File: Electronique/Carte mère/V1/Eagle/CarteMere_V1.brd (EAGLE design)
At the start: 95 x 80.1 mm, 25 parts, among them J100 BP_Rouge, J101 BP Jaune, J102 BP Vert, J600 LED_VERTE, J601 LED_JAUNE, J602 LED_ROUGE, Q500 SI2303DS, Q501 SI2302DS, U200 FIREBEETLE-ESP32-DFR0478, U300 RTC_ADA-3295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

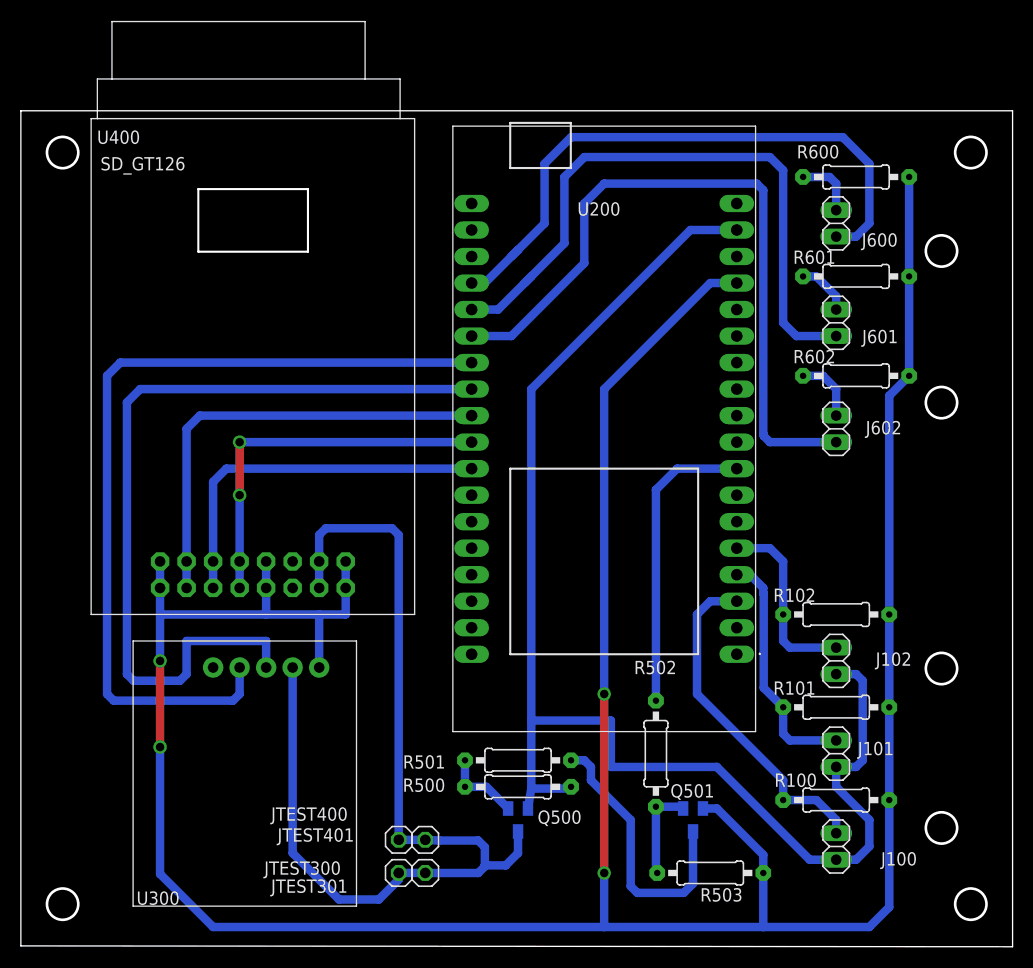
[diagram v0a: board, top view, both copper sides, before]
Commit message: Modificaiton du diamètre perçage vis et recréation des fichiers gerbers
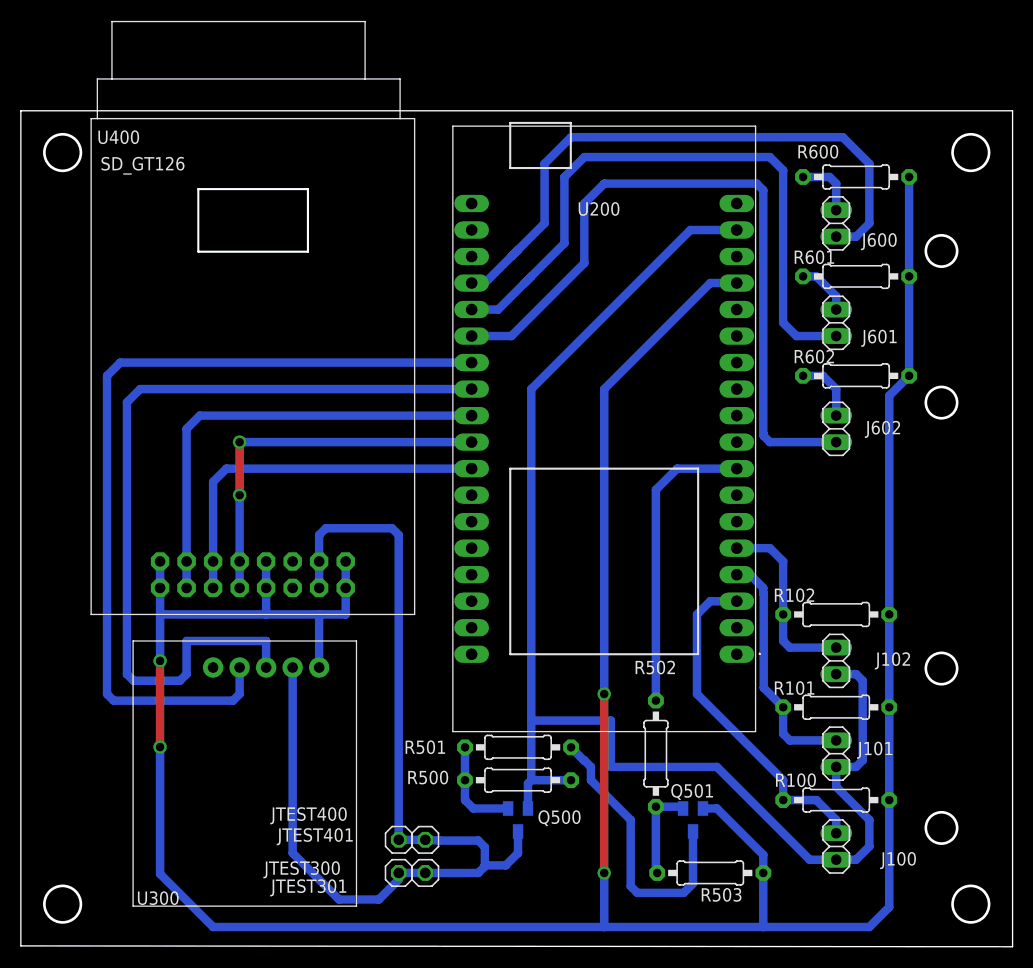
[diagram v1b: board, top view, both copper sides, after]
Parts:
- moved R501 1.24 mm to (47.6, 19.0)
- moved R500 0.63 mm to (47.6, 15.9)
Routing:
- net N$7: track 7.53 -> 9.52 mm
- net DQ501: track 26.8 -> 27.3 mm
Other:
- outline, holes or cut-outs redrawn
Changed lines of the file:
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@@
 <setting verticaltext="up"/>
 </settings>
-<grid distance="50" unitdist="mil" unit="mil" style="lines" multiple="1" display="no" altdistance="5" altunitdist="mm" altunit="mm"/>
+<grid distance="1" unitdist="mm" unit="mm" style="lines" multiple="1" display="no" altdistance="0.1" altunitdist="mm" altunit="mm"/>
 <layers>
 <layer number="1" name="Top" color="4" fill="1" visible="yes" active="yes"/>
@@
 <layer number="18" name="Vias" color="2" fill="1" visible="yes" active="yes"/>
 <layer number="19" name="Unrouted" color="6" fill="1" visible="yes" active="yes"/>
-<layer number="20" name="Dimension" color="24" fill="1" visible="no" active="yes"/>
+<layer number="20" name="Dimension" color="24" fill="1" visible="yes" active="yes"/>
 <layer number="21" name="tPlace" color="7" fill="1" visible="yes" active="yes"/>
 <layer number="22" name="bPlace" color="7" fill="1" visible="yes" active="yes"/>
-<layer number="23" name="tOrigins" color="15" fill="1" visible="no" active="yes"/>
-<layer number="24" name="bOrigins" color="15" fill="1" visible="no" active="yes"/>
+<layer number="23" name="tOrigins" color="15" fill="1" visible="yes" active="yes"/>
+<layer number="24" name="bOrigins" color="15" fill="1" visible="yes" active="yes"/>
 <layer number="25" name="tNames" color="7" fill="1" visible="yes" active="yes"/>
 <layer number="26" name="bNames" color="7" fill="1" visible="yes" active="yes"/>
@@
 <wire x1="95" y1="80" x2="0" y2="80" width="0" layer="20"/>
 <wire x1="0" y1="80" x2="0" y2="0" width="0" layer="20"/>
-<circle x="4" y="76" radius="1.5" width="0.254" layer="20"/>
-<circle x="91" y="76" radius="1.5" width="0.254" layer="20"/>
-<circle x="91" y="4" radius="1.5" width="0.254" layer="20"/>
-<circle x="4" y="4" radius="1.5" width="0.254" layer="20"/>
+<circle x="4" y="76" radius="1.75" width="0.254" layer="20"/>
+<circle x="91" y="76" radius="1.75" width="0.254" layer="20"/>
+<circle x="91" y="4" radius="1.75" width="0.254" layer="20"/>
+<circle x="4" y="4" radius="1.75" width="0.254" layer="20"/>
 <circle x="88.19" y="66.57" radius="1.5" width="0.254" layer="20"/>
 <circle x="88.19" y="52.045" radius="1.5" width="0.254" layer="20"/>
@@
 <dimension x1="4" y1="76" x2="17" y2="76" x3="10.5" y3="96.5" textsize="1.778" layer="47"/>
 <dimension x1="4" y1="76" x2="4" y2="72.5" x3="-22.5" y3="74.25" textsize="1.778" layer="47"/>
+<dimension x1="60.4266" y1="23.495" x2="60.4774" y2="23.495" x3="60.452" y3="23.495" textsize="1.778" layer="16"/>
+<dimension x1="60.4012" y1="23.5458" x2="60.8076" y2="23.6728" x3="60.684846875" y3="23.351865625" textsize="1.778" layer="16"/>
+<dimension x1="60.9092" y1="23.495" x2="62.2554" y2="23.4188" x3="61.543034375" y3="22.763259375" textsize="1.778" layer="16"/>
 </plain>
 <attributes>
@@
 <attribute name="VALUE" x="82.2706" y="55.245" size="1.27" layer="27" ratio="10" rot="R180"/>
 </element>
-<element name="R501" library="Eagle_UOF_Lib" package="0207/10" value="0R" x="47.625" y="17.78" smashed="yes" rot="R180">
-<attribute name="NAME" x="40.673" y="18.256" size="1.27" layer="25" ratio="10" rot="R180"/>
-<attribute name="VALUE" x="49.8856" y="18.415" size="1.27" layer="27" ratio="10" rot="R180"/>
-</element>
-<element name="R500" library="Eagle_UOF_Lib" package="0207/10" value="100k" x="47.625" y="15.24" smashed="yes">
-<attribute name="NAME" x="36.577" y="14.764" size="1.27" layer="25" ratio="10"/>
-<attribute name="VALUE" x="45.3644" y="14.605" size="1.27" layer="27" ratio="10"/>
-</element>
 <element name="Q500" library="Eagle_UOF_Lib" package="SOT23" value="SI2303DS" x="47.625" y="12.065" smashed="yes" rot="MR180">
 <attribute name="NAME" x="53.72" y="12.97" size="1.27" layer="25" rot="R180"/>
@@
 <attribute name="NAME" x="24.5837" y="9.9896" size="1.27" layer="25" ratio="10"/>
 <attribute name="VALUE" x="37.4699" y="6.9858" size="1.27" layer="27"/>
+</element>
+<element name="R501" library="Eagle_UOF_Lib" package="0207/10" value="0R" x="47.6277" y="19.0205" smashed="yes" rot="R180">
+<attribute name="NAME" x="40.7824" y="19.6682" size="1.27" layer="25" ratio="10" rot="R180"/>
+<attribute name="VALUE" x="47.4626" y="19.6047" size="1.27" layer="27" ratio="10" rot="R180"/>
+</element>
+<element name="R500" library="Eagle_UOF_Lib" package="0207/10" value="100k" x="47.625" y="15.875" smashed="yes">
+<attribute name="NAME" x="36.957" y="15.494" size="1.27" layer="25" ratio="10"/>
+<attribute name="VALUE" x="45.9994" y="15.24" size="1.27" layer="27" ratio="10"/>
 </element>
 </elements>
@@
 <signal name="3V3">
 <contactref element="U200" pad="17"/>
-<contactref element="R500" pad="2"/>
 <contactref element="Q500" pad="2"/>
-<wire x1="48.895" y1="15.07" x2="48.575" y2="13.165" width="0.8128" layer="16"/>
-<wire x1="48.895" y1="21.59" x2="48.895" y2="15.07" width="0.8128" layer="16"/>
+<wire x1="48.895" y1="21.59" x2="48.895" y2="15.875" width="0.8128" layer="16"/>
 <contactref element="J101" pad="1"/>
 <contactref element="J102" pad="1"/>
@@
 <wire x1="48.895" y1="21.59" x2="48.895" y2="53.34" width="0.8128" layer="16"/>
 <wire x1="56.515" y1="17.145" x2="66.675" y2="17.145" width="0.8128" layer="16"/>
-<wire x1="52.705" y1="15.24" x2="52.535" y2="15.07" width="0.8128" layer="16"/>
-<wire x1="52.535" y1="15.07" x2="48.895" y2="15.07" width="0.8128" layer="16"/>
 <wire x1="66.675" y1="17.145" x2="75.565" y2="8.255" width="0.8128" layer="16"/>
 <wire x1="75.565" y1="8.255" x2="78.105" y2="8.255" width="0.8128" layer="16"/>
@@
 <wire x1="48.895" y1="53.34" x2="64.135" y2="68.58" width="0.8128" layer="16"/>
 <wire x1="64.135" y1="68.58" x2="68.58" y2="68.58" width="0.8128" layer="16"/>
+<contactref element="R500" pad="2"/>
+<wire x1="52.705" y1="15.875" x2="52.875" y2="15.875" width="0.8128" layer="16"/>
+<wire x1="48.575" y1="13.165" x2="48.575" y2="15.555" width="0.8128" layer="16"/>
+<wire x1="48.575" y1="15.555" x2="48.895" y2="15.875" width="0.8128" layer="16"/>
+<wire x1="48.895" y1="15.875" x2="52.705" y2="15.875" width="0.8128" layer="16"/>
 </signal>
 <signal name="BP_VERT">
@@
 <signal name="DQ501">
 <contactref element="Q501" pad="3"/>
-<contactref element="R501" pad="1"/>
-<wire x1="52.705" y1="17.78" x2="53.975" y2="17.78" width="0.8128" layer="16"/>
 <wire x1="64.389" y1="10.965" x2="64.389" y2="5.969" width="0.8128" layer="16"/>
 <wire x1="53.975" y1="17.78" x2="54.61" y2="17.145" width="0.8128" layer="16"/>
@@
 <wire x1="58.42" y1="5.715" x2="58.42" y2="12.065" width="0.8128" layer="16"/>
 <wire x1="58.42" y1="12.065" x2="54.61" y2="15.875" width="0.8128" layer="16"/>
+<contactref element="R501" pad="1"/>
+<wire x1="52.7077" y1="19.0205" x2="53.9455" y2="17.7505" width="0.8128" layer="16"/>
+<wire x1="53.9455" y1="17.7505" x2="53.975" y2="17.78" width="0.8128" layer="16"/>
 </signal>
 <signal name="LED_VERTE">
@@
 </signal>
 <signal name="N$7">
+<contactref element="Q500" pad="1"/>
 <contactref element="R501" pad="2"/>
 <contactref element="R500" pad="1"/>
-<contactref element="Q500" pad="1"/>
-<wire x1="42.545" y1="17.78" x2="42.545" y2="15.24" width="0.8128" layer="16"/>
-<wire x1="42.545" y1="15.24" x2="44.6" y2="15.24" width="0.8128" layer="16"/>
-<wire x1="44.6" y1="15.24" x2="46.675" y2="13.165" width="0.8128" layer="16"/>
+<wire x1="46.675" y1="13.165" x2="43.35" y2="13.165" width="0.8128" layer="16"/>
+<wire x1="43.35" y1="13.165" x2="42.545" y2="13.97" width="0.8128" layer="16"/>
+<wire x1="42.545" y1="13.97" x2="42.545" y2="15.875" width="0.8128" layer="16"/>
+<wire x1="42.545" y1="15.875" x2="42.5477" y2="15.8777" width="0.8128" layer="16"/>
+<wire x1="42.5477" y1="15.8777" x2="42.5477" y2="19.0205" width="0.8128" layer="16"/>
 </signal>
 <signal name="PWR_EN">
